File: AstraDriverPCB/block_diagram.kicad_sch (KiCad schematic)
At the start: 36 parts, among them CN1 JST VH 8 PIN, CN2 JST VH 2 PIN, CN3 JST VH 2 PIN, CN4 JST VH 2 PIN, CN5 JST VH 2 PIN

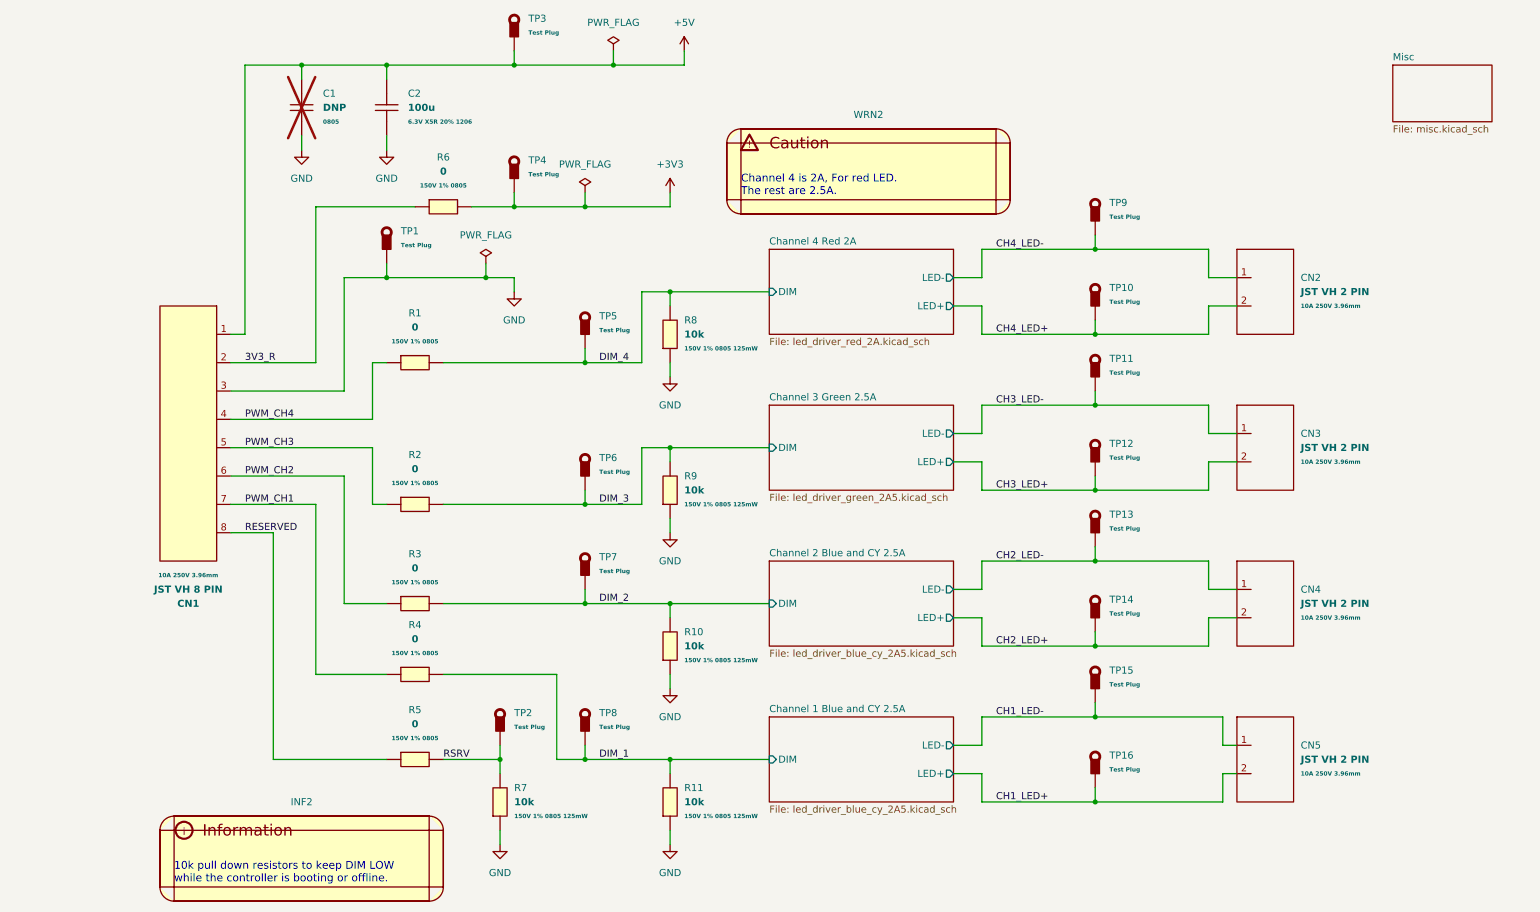
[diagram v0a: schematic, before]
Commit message: Added another 2 PIN VH connector for power, cleanup
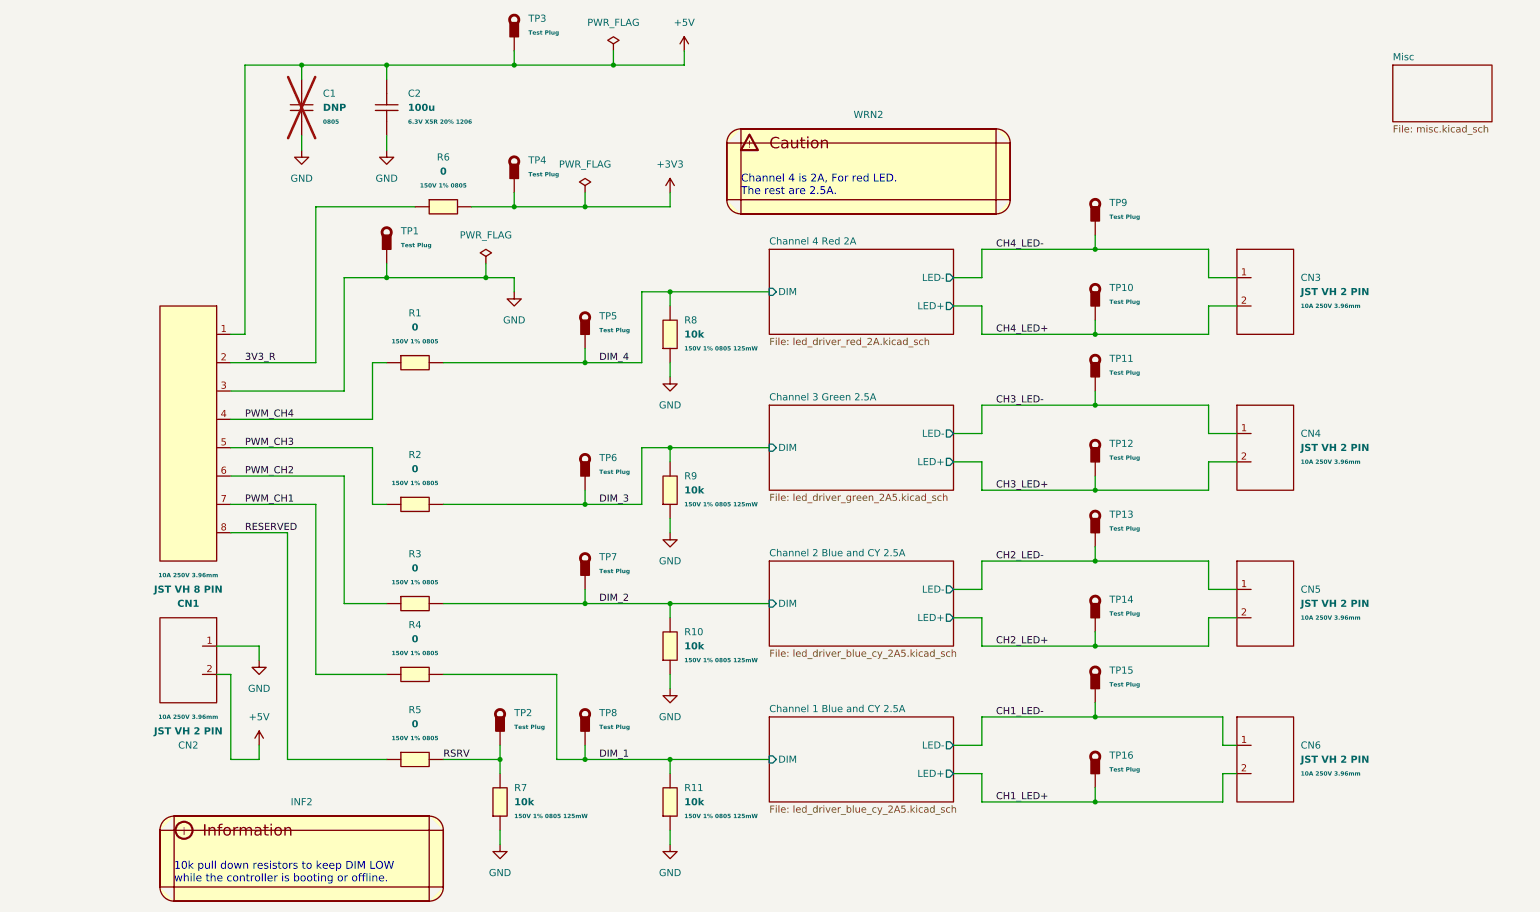
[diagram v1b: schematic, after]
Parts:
- added CN2: JST VH 2 PIN, LiveAstra:JST_VH_B2P-VH-B_1x02_P3.96mm_Vertical, symbol LiveAstra:JST_VH_2PIN_10A_250V
- renumbered CN2 to CN3, CN3 to CN4, CN4 to CN5, CN5 to CN6
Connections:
- net +5V: now also CN2.2
- net GND: now also CN2.1

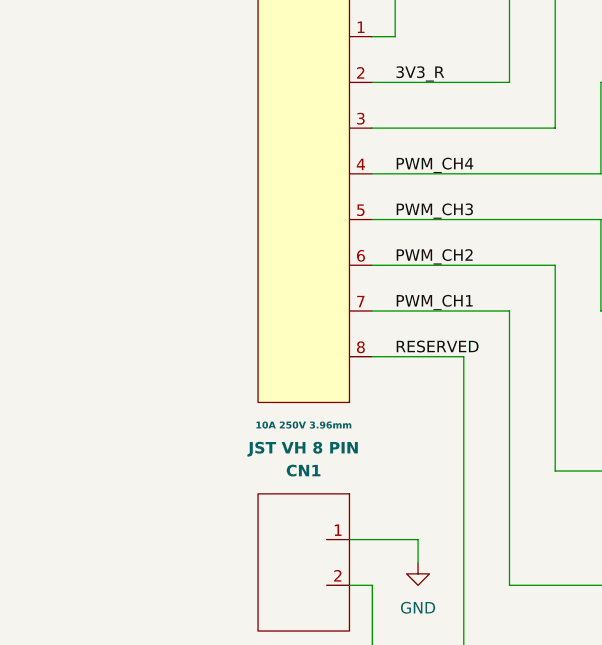
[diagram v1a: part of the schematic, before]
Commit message: Update vh to clone
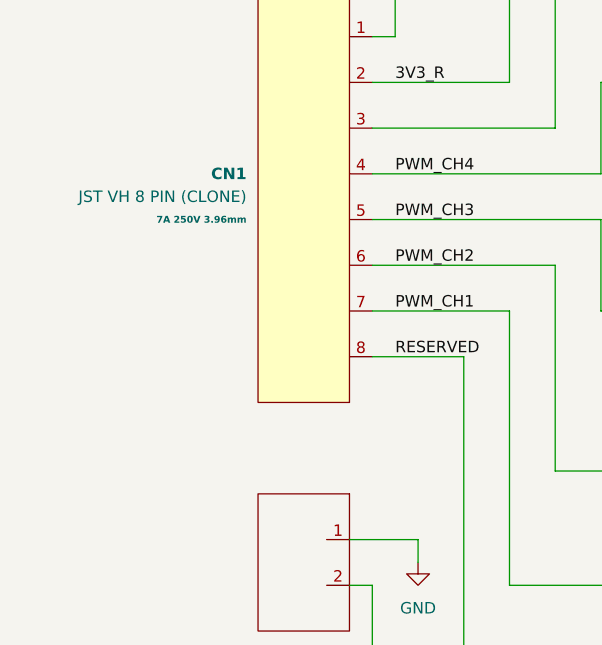
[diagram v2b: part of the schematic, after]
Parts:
- removed CN1: JST VH 8 PIN, LiveAstra:JST_VH_B8P-VH-B_1x08_P3.96mm_Vertical, symbol LiveAstra:JST_VH_8PIN_10A_250V
- added CN1: JST VH 8 PIN (CLONE), LiveAstra:JST_VH_CLONE_B8P-VH-B_1x08_P3.96mm_Vertical, symbol LiveAstra:JST_VH_8PIN_7A_250V_CLONE
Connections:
- net +5V: now also CN1.1
- net 3V3_R: now also CN1.2
- net GND: now also CN1.3
- net PWM_CH1: now also CN1.7
- net PWM_CH2: now also CN1.6
- net PWM_CH3: now also CN1.5
- net PWM_CH4: now also CN1.4
- net RESERVED: now also CN1.8
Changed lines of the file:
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@@
+	)
+	(symbol
+		(lib_id "LiveAstra:JST_VH_8PIN_7A_250V_CLONE")
+		(at 30.48 91.44 0)
+		(mirror y)
+		(unit 1)
+		(exclude_from_sim no)
+		(in_bom yes)
+		(on_board yes)
+		(dnp no)
+		(property "Reference" "CN1"
+			(at 24.13 88.9 0)
+			(effects
+				(font
+					(size 1.27 1.27)
+					(bold yes)
+				)
+				(justify left)
+			)
+		)
+		(property "Value" "JST VH 8 PIN (CLONE)"
+			(at 24.13 91.4399 0)
+			(effects
+				(font
+					(size 1.27 1.27)
+				)
+				(justify left)
+			)
+		)
+		(property "Footprint" "LiveAstra:JST_VH_CLONE_B8P-VH-B_1x08_P3.96mm_Vertical"
+			(at 30.48 124.46 0)
+			(effects
+				(font
+					(size 1.27 1.27)
+				)
+				(hide yes)
+			)
+		)
+		(property "Datasheet" "https://lcsc.com/product-detail/Others_Changjiang-Connectors-A3963WV-8P_C239415.html"
+			(at 30.48 119.38 0)
+			(effects
+				(font
+					(size 1.27 1.27)
+				)
+				(hide yes)
+			)
+		)
+		(property "Description" "1x8P 8P VH 1 3.96mm 8 Brass Plugin,P=3.96mm Wire To Board Connector ROHS"
+			(at 30.48 134.62 0)
+			(effects
+				(font
+					(size 1.27 1.27)
+				)
+				(hide yes)
+			)
+		)
+		(property "LCSC Part" "C239415"
+			(at 30.48 139.7 0)
+			(effects
+				(font
+					(size 1.27 1.27)
+				)
+				(hide yes)
+			)
+		)
+		(property "MPN" "A3963WV-8P"
+			(at 30.48 124.46 0)
+			(effects
+				(font
+					(size 1.27 1.27)
+				)
+				(hide yes)
+			)
+		)
+		(property "MFN" "CJT(Changjiang Connectors)"
+			(at 30.48 129.54 0)
+			(effects
+				(font
+					(size 1.27 1.27)
+				)
+				(hide yes)
+			)
+		)
+		(property "Extra Values" "7A 250V 3.96mm"
+			(at 24.13 93.9799 0)
+			(effects
+				(font
+					(size 0.762 0.762)
+					(bold yes)
+				)
+				(justify left)
+			)
+		)
+		(pin "2"
+		)
+		(pin "8"
+		)
+		(pin "7"
+		)
+		(pin "4"
+		)
+		(pin "6"
+		)
+		(pin "5"
+		)
+		(pin "1"
+		)
+		(pin "3"
+		)
+		(instances
+			(project ""
+				(path "/d8760d88-6646-4dd8-a980-02e776803cc5/db9d16fd-00a9-4695-9dd4-6de80f9e2ffc"
+					(reference "CN1")
+					(unit 1)
+				)
+			)
+		)
 	)
 	(symbol
@@
 					(unit 1)
 				)
-			)
-		)
-	)
-	(symbol
-		(lib_id "LiveAstra:JST_VH_8PIN_10A_250V")
-		(at 30.48 91.44 0)
-		(mirror y)
-		(unit 1)
-		(exclude_from_sim no)
-		(in_bom yes)
-		(on_board yes)
-		(dnp no)
-		(property "Reference" "CN1"
-			(at 30.48 121.92 0)
-			(effects
-				(font
-					(size 1.27 1.27)
-					(bold yes)
-				)
-			)
-		)
-		(property "Value" "JST VH 8 PIN"
-			(at 30.48 119.38 0)
-			(effects
-				(font
-					(size 1.27 1.27)
-					(bold yes)
-				)
-			)
-		)
-		(property "Footprint" "LiveAstra:JST_VH_B8P-VH-B_1x08_P3.96mm_Vertical"
-			(at 30.48 124.46 0)
-			(effects
-				(font
-					(size 1.27 1.27)
-				)
-				(hide yes)
-			)
-		)
-		(property "Datasheet" "https://lcsc.com/product-detail/_JST-Sales-America_B8P-VH-B-LF-SN_JST-Sales-America-B8P-VH-B-LF-SN_C265117.html"
-			(at 30.48 129.54 0)
-			(effects
-				(font
-					(size 1.27 1.27)
-				)
-				(hide yes)
-			)
-		)
-		(property "Description" "1x8P 8P VH Tin 8 -25℃~+85℃ 10A 1 3.96mm Brass Direct Insert Plugin,P=3.96mm Wire To Board Connector ROHS"
-			(at 30.48 81.28 0)
-			(effects
-				(font
-					(size 1.27 1.27)
-				)
-				(hide yes)
-			)
-		)
-		(property "LCSC Part" "C265117"
-			(at 30.48 134.62 0)
-			(effects
-				(font
-					(size 1.27 1.27)
-				)
-				(hide yes)
-			)
-		)
-		(property "Extra Values" "10A 250V 3.96mm"
-			(at 30.48 116.84 0)
-			(effects
-				(font
-					(size 0.762 0.762)
-					(bold yes)
-				)
-			)
-		)
-		(property "MPN" "B8P-VH-B(LF)(SN)"
-			(at 30.48 138.43 0)
-			(effects
-				(font
-					(size 1.27 1.27)
-				)
-				(hide yes)
-			)
-		)
-		(property "MFN" "JST"
-			(at 30.48 142.24 0)
-			(effects
-				(font
-					(size 1.27 1.27)
-				)
-				(hide yes)
-			)
-		)
-		(pin "6"
-		)
-		(pin "2"
-		)
-		(pin "8"
-		)
-		(pin "1"
-		)
-		(pin "7"
-		)
-		(pin "5"
-		)
-		(pin "3"
-		)
-		(pin "4"
-		)
-		(instances
-			(project ""
-				(path "/d8760d88-6646-4dd8-a980-02e776803cc5/db9d16fd-00a9-4695-9dd4-6de80f9e2ffc"
-					(reference "CN1")
-					(unit 1)
-				)
